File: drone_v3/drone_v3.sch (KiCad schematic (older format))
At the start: 1 part, among them U1 STM32F405RGTx

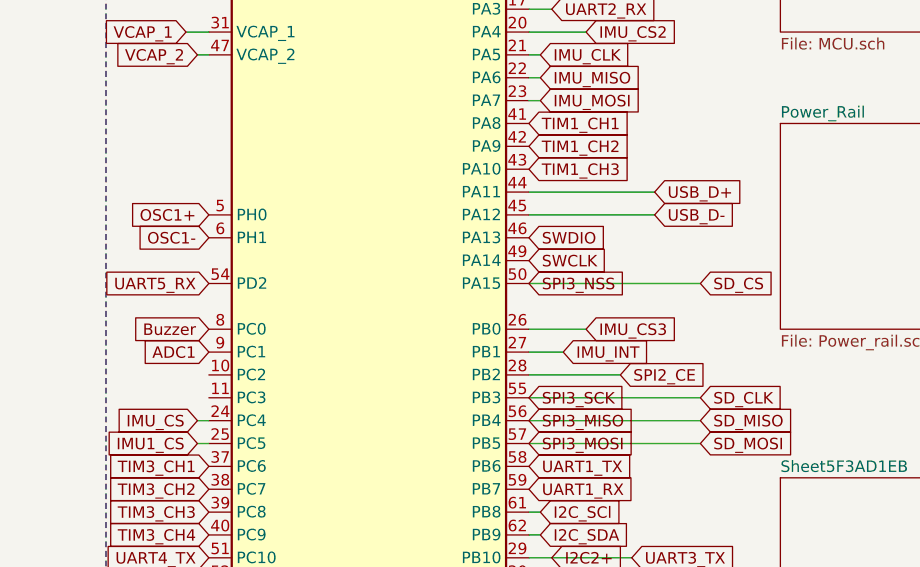
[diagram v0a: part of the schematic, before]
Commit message: change 20602 to 20948, ms5611 to bmp180
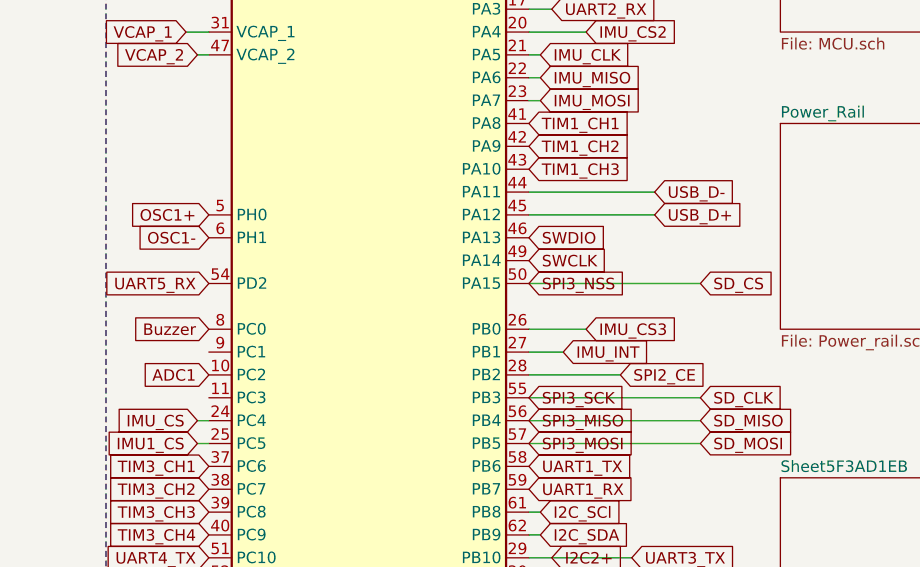
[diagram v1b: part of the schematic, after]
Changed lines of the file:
@@
 Text GLabel 2600 3800 2    50   Input ~ 0
 SPI3_MOSI
-Text GLabel 1200 3400 0    50   Input ~ 0
+Text GLabel 1200 3500 0    50   Input ~ 0
 ADC1
 Text GLabel 900  5100 2    50   Input ~ 0
@@
 Text GLabel 1150 3800 0    50   Input ~ 0
 IMU1_CS
+Text GLabel 3150 2700 2    50   Input ~ 0
+USB_D-
 Text GLabel 3150 2800 2    50   Input ~ 0
-USB_D-
-Text GLabel 3150 2700 2    50   Input ~ 0
 USB_D+
 Wire Wire Line
-	3150 2800 2600 2800
+	3150 2700 2600 2700
 Wire Wire Line
-	2600 2700 3150 2700
+	2600 2800 3150 2800
 Text GLabel 2850 2000 2    50   Input ~ 0
 IMU_CS2
